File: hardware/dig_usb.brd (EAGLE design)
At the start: 146.1 x 102.6 mm, 123 parts, among them IC201 ATMEGA32A-AU, IC202 DS1337S, IC203 MAX487CSA, IC204 74HC166D, IC205 74HC595D, IC301 LTV-356T, IC302 LTV-356T, IC303 LTV-356T, IC304 LTV-356T, IC305 LTV-356T, IC306 LTV-356T, IC307 LTV-356T, IC308 LTV-356T, K401 S202S02, K402 S202S02, K403 S202S02, K404 S202S02, K405 S202S02, K406 S202S02, K407 S202S02, K408 S202S02, Q201 32,768kHz, T301 BCR191, T302 BCR191, T303 BCR191, T304 BCR191, T305 BCR191, T306 BCR191, T307 BCR191, T308 BCR191, X101 RIA-73-02, X201 ISP, X202 RIA-73-02, X301 RIA-73-02, X302 RIA-73-02, X303 RIA-73-02, X304 RIA-73-02, X305 RIA-73-02, X401 RIA-73-02, X402 RIA-73-02, X403 RIA-73-02, X404 RIA-73-02, X405 RIA-73-02

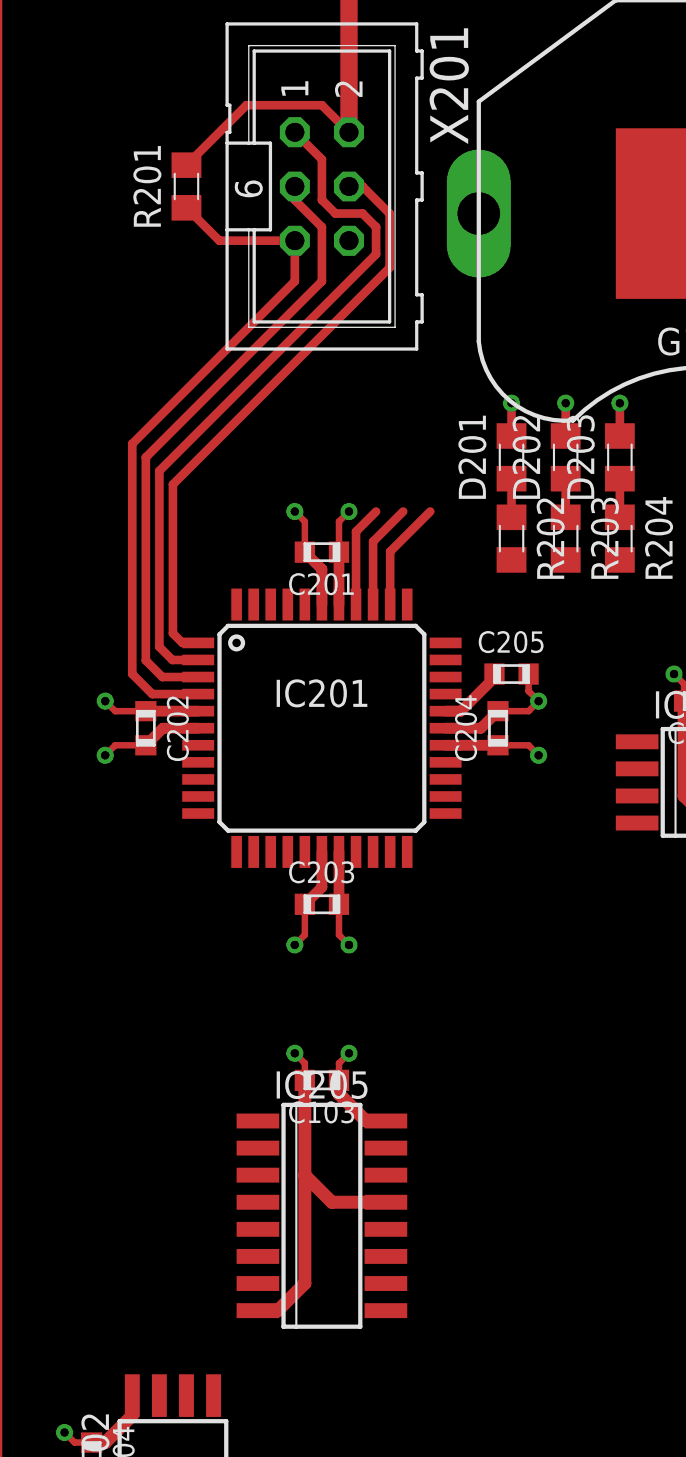
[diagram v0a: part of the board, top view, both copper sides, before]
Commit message: dig_usb auf AT90USB1287 umgestellt
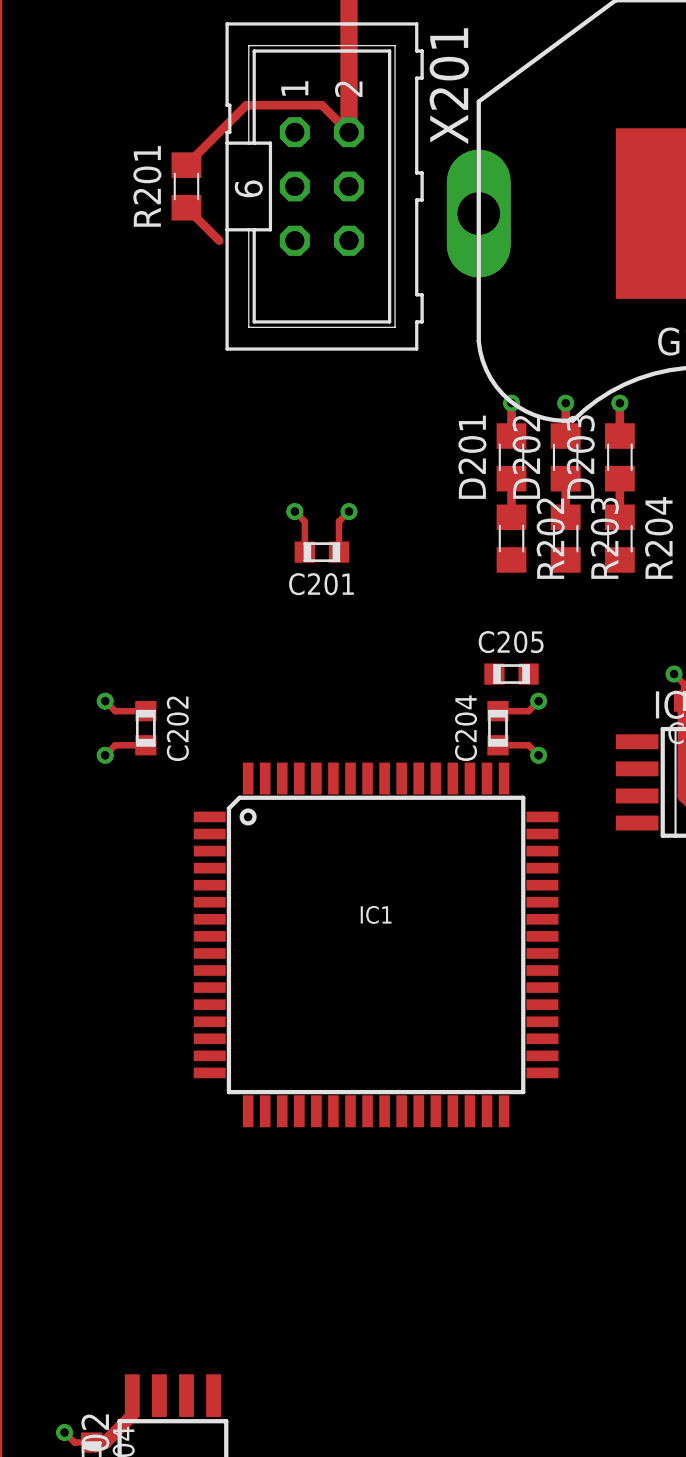
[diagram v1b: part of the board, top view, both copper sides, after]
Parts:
- removed C103, C203: 100nF, passiv:CHIP_0603
- removed IC201: ATMEGA32A-AU, ic-mcu:QFP44_08
- removed IC205: 74HC595D, ic-logik:SOP16_127
- added IC1: AT90USB1287-AU, ic-mcu:QFP64_08
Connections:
- removed net DO: IC201.44, IC205.14
- removed net N$25: C205.1, IC201.29
- removed net N$42: IC201.4, R201.1, X201.RESET
- removed net N$61: IC201.30, R205.1, R206.1
- removed net N$8: IC201.35, R204.2
- removed net N$90: IC201.37, R202.2
- removed net N$92: IC201.36, R203.2
- new net !RESET: IC1.20, R201.1, X201.RESET
- new net LED1: IC1.15, R202.2
- new net LED2: IC1.16, R203.2
- new net LED3: IC1.17, R204.2
- new net N$12: C205.1, IC1.62
- new net OUT0: IC1.51
- new net OUT1: IC1.50
- new net OUT2: IC1.49
- new net OUT3: IC1.48
- new net OUT4: IC1.47
- new net OUT5: IC1.46
- new net OUT6: IC1.45
- new net OUT7: IC1.44
- new net TEMP: IC1.54, R205.1, R206.1
- new net UGND: IC1.6
- new net UVCC: IC1.3
- new net VBUS: IC1.8
- net !R: now also IC1.33; no longer IC201.40, IC205.10
- net +5V: now also IC1.21, IC1.52, IC1.64; no longer C103.1, C203.1, IC201.17, IC201.27, IC201.38, IC201.5, IC205.16
- net ALARM1: now also IC1.18; no longer IC201.11
- net ALARM2: now also IC1.19; no longer IC201.12
- net BAT: now also IC1.55; no longer IC201.31
- net C1: now also IC1.31; no longer IC201.41, IC205.11
- net C2: now also IC1.32; no longer IC201.42, IC205.12
- net DI: now also IC1.34; no longer IC201.43
- net GND: now also IC1.22, IC1.53, IC1.63; no longer C103.2, C203.2, IC201.18, IC201.28, IC201.39, IC201.6, IC205.13, IC205.8
- net IN0: now also IC1.35; no longer IC201.19
- net IN1: now also IC1.36; no longer IC201.20
- net IN2: now also IC1.37; no longer IC201.21
- net IN3: now also IC1.38; no longer IC201.22
- net IN4: now also IC1.39; no longer IC201.23
- net IN5: now also IC1.40; no longer IC201.24
- net IN6: now also IC1.41; no longer IC201.25
- net IN7: now also IC1.42; no longer IC201.26
- net MISO: now also IC1.13; no longer IC201.2
- net MOSI: now also IC1.12; no longer IC201.1
- net RE: now also IC1.30; no longer IC201.14
- net RXD: now also IC1.27; no longer IC201.9
- net SCK: now also IC1.11; no longer IC201.3
- net SCL: now also IC1.25; no longer IC201.15
- net SDA: now also IC1.26; no longer IC201.16
- net TE: now also IC1.29; no longer IC201.13
- net TXD: now also IC1.28; no longer IC201.10
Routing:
- net MISO: track 32.7 -> 0.00 mm
- net N$42: track 32.7 -> 0.00 mm
- net GND: track 93.6 -> 61.2 mm, vias 13 -> 11
- net SCK: track 28.9 -> 0.00 mm
- net MOSI: track 27.7 -> 0.00 mm
- net +5V: track 376.0 -> 359.0 mm, vias 7 -> 5
- net N$8: track 5.14 -> 0.00 mm
- net N$92: track 4.94 -> 0.00 mm
- net N$90: track 4.75 -> 0.00 mm
- net N$25: track 3.11 -> 0.00 mm
- net !RESET: track 0.00 -> 2.18 mm

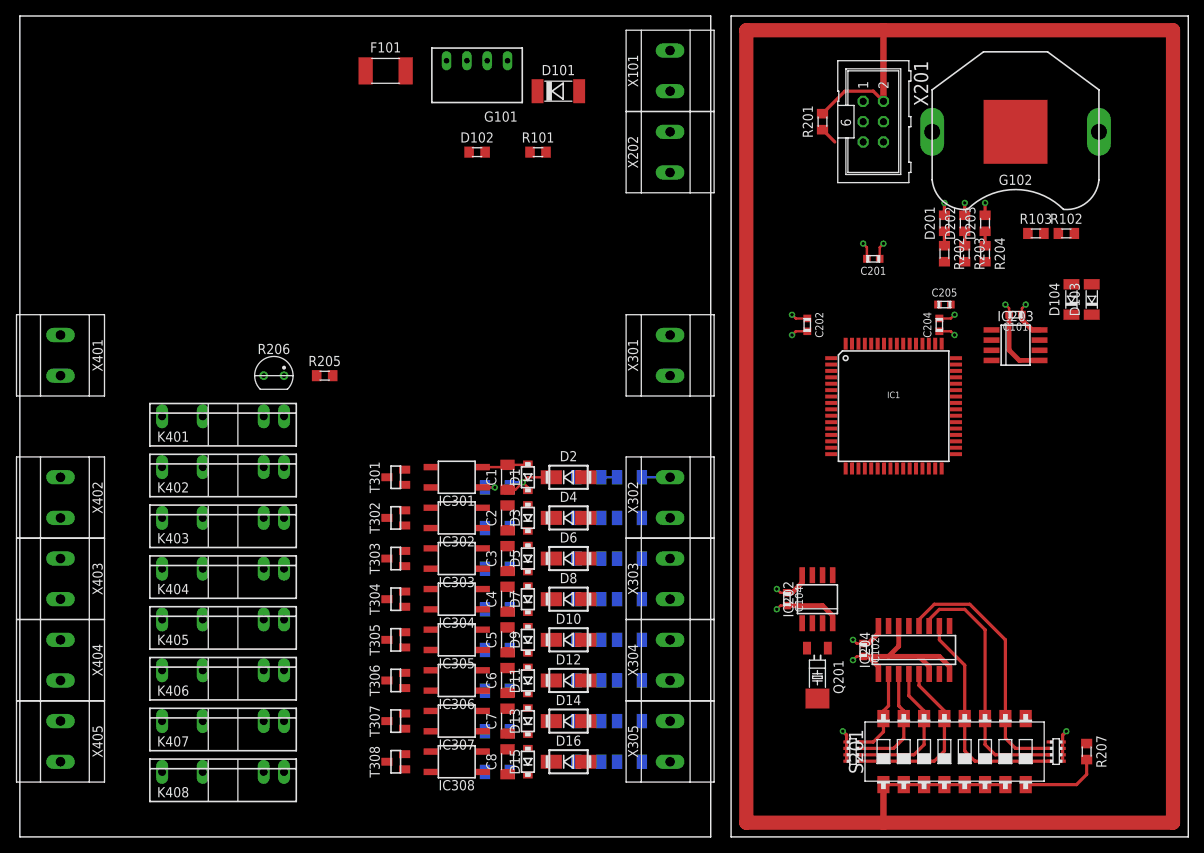
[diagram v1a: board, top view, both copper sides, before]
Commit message: IO Bereich der unteren Platine geroutet
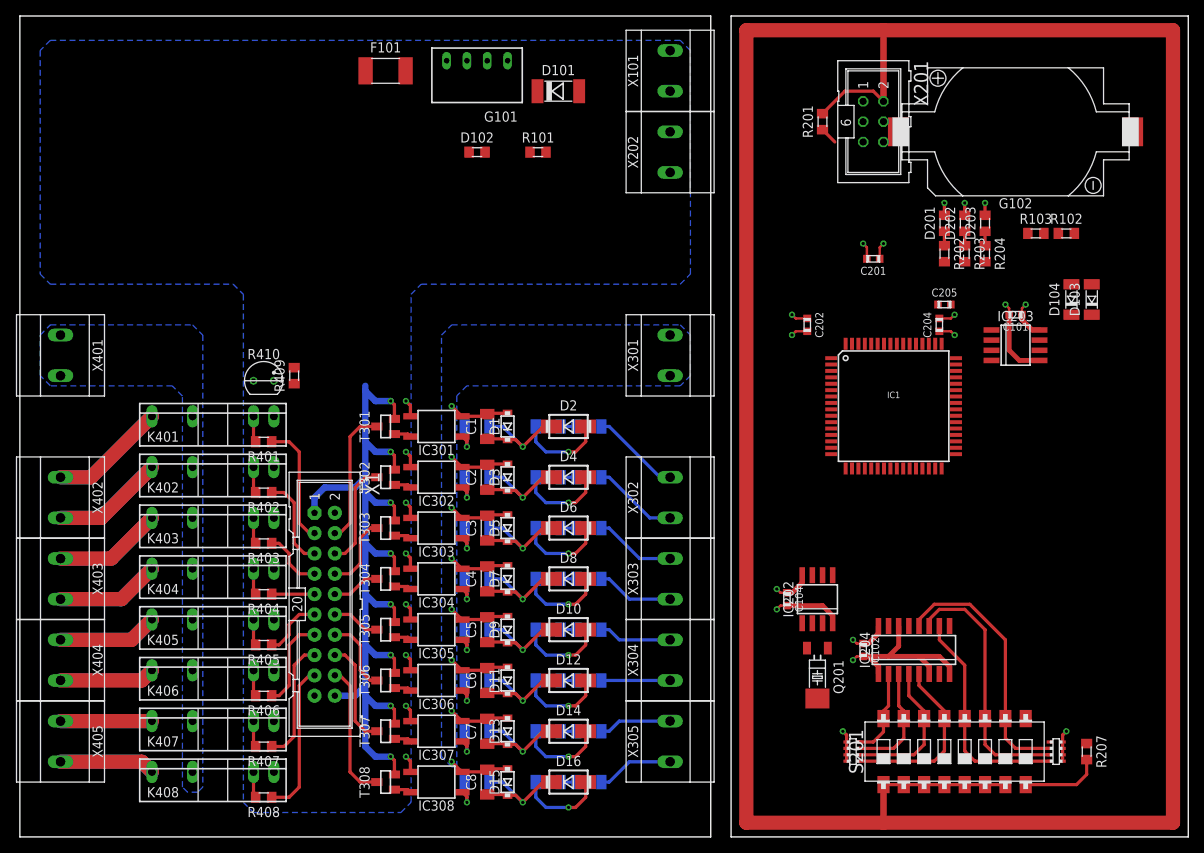
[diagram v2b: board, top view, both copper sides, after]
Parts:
- removed R205: 3,3kΩ, passiv:CHIP_0805
- removed R206: KTY81-210, sensor:TO92
- added R401, R402, R403, R404, R405, R406, R407, R408: (no value), passiv:CHIP_0805
- added R409: 3,3kΩ, passiv:CHIP_0805
- added R410: KTY81-210, sensor:TO92
- added X1: (no value), anschluss:WS20V
- G102: value KZH20P -> KZH20SMD-2; device batterie:KZH20P -> batterie:KHZ20SMD-2
- moved R1 8.13 mm to (66.0, 50.8)
- moved R2 8.13 mm to (71.1, 50.8)
- moved R3 8.03 mm to (57.1, 50.8)
- moved R4 7.18 mm to (66.0, 44.5)
- moved R5 7.18 mm to (71.1, 44.5)
- moved R6 6.84 mm to (57.1, 44.5)
- moved C1 6.84 mm to (58.4, 50.8)
- moved D1 6.84 mm to (61.0, 50.8)
- moved IC301 6.84 mm to (52.1, 50.8)
- moved T301 6.48 mm to (45.7, 50.8)
- moved R7 6.35 mm to (66.0, 38.1)
- moved R8 6.35 mm to (71.1, 38.1)
- moved D2 6.35 mm to (68.6, 50.8)
- moved C2 5.68 mm to (58.4, 44.5)
- moved D3 5.68 mm to (61.0, 44.5)
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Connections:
- new net N$100: T307.3, X1.16
- new net N$101: T308.3, X1.18
- new net N$16: K402.3, R402.2
- new net N$25: K403.3, R403.2
- new net N$37: K404.3, R404.2
- new net N$42: K405.3, R405.2
- new net N$50: K406.3, R406.2
- new net N$61: K407.3, R407.2
- new net N$66: K408.3, R408.2
- new net N$67: R401.1, X1.3
- new net N$79: R402.1, X1.5
- new net N$8: K401.3, R401.2
- new net N$87: R403.1, X1.7
- new net N$88: R404.1, X1.9
- new net N$90: R405.1, X1.11
- new net N$91: R406.1, X1.13
- new net N$92: R407.1, X1.15
- new net N$93: R408.1, X1.17
- new net N$94: T301.3, X1.4
- new net N$95: T302.3, X1.6
- new net N$96: T303.3, X1.8
- new net N$97: T304.3, X1.10
- new net N$98: T305.3, X1.12
- new net N$99: T306.3, X1.14
- net +5V: now also R409.2, X1.1, X1.20; no longer R205.2
- net GND: now also G102.-, R410.2, X1.19, X1.2; no longer G102.N, R206.2
- net IN0: no longer T301.3
- net IN1: no longer T302.3
- net IN2: no longer T303.3
- net IN3: no longer T304.3
- net IN4: no longer T305.3
- net IN5: no longer T306.3
- net IN6: no longer T307.3
- net IN7: no longer T308.3
- net N$21: now also G102.+; no longer G102.P1, G102.P2
- net TEMP: now also R409.1, R410.1; no longer R205.1, R206.1
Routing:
- net +5V: track 359.0 -> 466.6 mm, vias 5 -> 13
- net GNDIO: track 5.80 -> 61.3 mm, vias 0 -> 8
- net N$68: track 0.00 -> 29.2 mm
- net N$72: track 0.00 -> 28.1 mm
- net N$74: track 0.00 -> 27.1 mm
- net N$76: track 0.00 -> 26.0 mm
- net N$78: track 0.00 -> 25.0 mm
- net N$89: track 0.00 -> 23.9 mm
- net N$82: track 0.00 -> 23.9 mm
- net N$84: track 0.00 -> 22.9 mm
- net N$93: track 0.00 -> 19.1 mm
- net N$101: track 0.00 -> 17.1 mm
- net N$94: track 0.00 -> 17.1 mm
- net GND: track 61.2 -> 78.2 mm, vias 11 -> 19
- net N$92: track 0.00 -> 15.3 mm
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- added copper zone on layer 16, net GNDIO
- added copper zone on layer 16, net L

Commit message: Einiges auf dig_usb controllerboard gerouted
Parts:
- removed R101, R202, R203, R204: 390Ω, passiv:CHIP_0805
- added D17, D18, D19, D20, D21, D22, D23, D24, D25, D26, D27, D28, D29, D30, D31, D32: GN, led:CHIP_0805
- added R25, R26, R27, R28, R29: 1,5kΩ, widerstandsnetzwerk:1206
- added X2: (no value), anschluss:WS20V
- R401, R402, R403, R404, R405, R406, R407, R408: value (none) -> 470Ω
- moved Q201 94.1 mm to (22.2, 74.9), turned to 90 degrees
- moved IC202 83.5 mm to (29.8, 74.9), turned to 270 degrees
- moved C104 82.6 mm to (29.8, 78.7), turned to 180 degrees
- moved C101 43.8 mm to (123.2, 21.0), turned to 270 degrees
- moved D102 43.5 mm to (99.7, 76.2), turned to 90 degrees
- moved IC203 40.1 mm to (127.0, 21.0), turned to 0 degrees
- moved C202 23.4 mm to (121.3, 58.4), turned to 90 degrees
- moved D203 18.4 mm to (102.2, 76.2)
- moved D202 13.3 mm to (104.8, 76.2)
- moved R103 12.8 mm to (132.7, 63.5), turned to 90 degrees
- moved R102 12.3 mm to (135.3, 63.5), turned to 90 degrees
- moved C201 9.92 mm to (100.3, 64.1), turned to 270 degrees
- moved IC1 8.35 mm to (110.5, 61.6), turned to 270 degrees
- moved D201 8.25 mm to (107.3, 76.2)
- moved C204 6.87 mm to (120.7, 67.3), turned to 270 degrees
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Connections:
- new net N$102: D17.1, R25.1B
- new net N$103: D18.1, R25.2B
- new net N$104: D19.1, R25.3B
- new net N$105: D20.1, R25.4B
- new net N$106: D21.1, R26.1B
- new net N$107: D22.1, R26.2B
- new net N$108: D23.1, R26.3B
- new net N$109: D24.1, R26.4B
- new net N$110: D25.1, R27.1A
- new net N$111: D26.1, R27.2A
- new net N$112: D27.1, R27.3A
- new net N$113: D28.1, R27.4A
- new net N$114: D29.1, R28.1A
- new net N$115: D30.1, R28.2A
- new net N$116: D31.1, R28.3A
- new net N$117: D32.1, R28.4A
- net +5V: now also R29.4B, X2.1, X2.20; no longer R101.2
- net GND: now also D17.2, D18.2, D19.2, D20.2, D21.2, D22.2, D23.2, D24.2, D25.2, D26.2, D27.2, D28.2, D29.2, D30.2, D31.2, D32.2, X2.19, X2.2
- net IN0: now also R25.1A, X2.4
- net IN1: now also R25.2A, X2.6
- net IN2: now also R25.3A, X2.8
- net IN3: now also R25.4A, X2.10
- net IN4: now also R26.1A, X2.12
- net IN5: now also R26.2A, X2.14
- net IN6: now also R26.3A, X2.16
- net IN7: now also R26.4A, X2.18
- net LED1: now also R29.1B; no longer R202.2
- net LED2: now also R29.2B; no longer R203.2
- net LED3: now also R29.3B; no longer R204.2
- net N$4: now also R29.3A; no longer R204.1
- net N$44: now also R29.4A; no longer R101.1
- net N$62: now also R29.1A; no longer R202.1
- net N$63: now also R29.2A; no longer R203.1
- net OUT0: now also R27.1B, X2.3
- net OUT1: now also R27.2B, X2.5
- net OUT2: now also R27.3B, X2.7
- net OUT3: now also R27.4B, X2.9
- net OUT4: now also R28.1B, X2.11
- net OUT5: now also R28.2B, X2.13
- net OUT6: now also R28.3B, X2.15
- net OUT7: now also R28.4B, X2.17
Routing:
- net +5V: track 466.6 -> 600.6 mm, vias 13 -> 16
- net RXD: track 0.00 -> 83.5 mm, vias 0 -> 2
- net TXD: track 0.00 -> 83.0 mm, vias 0 -> 2
- net TE: track 0.00 -> 78.8 mm, vias 0 -> 2
- net RE: track 0.00 -> 74.7 mm, vias 0 -> 2
- net C1: track 0.00 -> 55.4 mm, vias 0 -> 2
- net GND: track 78.2 -> 130.4 mm
- net OUT7: track 0.00 -> 45.0 mm, vias 0 -> 2
- net IN7: track 0.00 -> 44.1 mm, vias 0 -> 1
- net DI: track 0.00 -> 42.8 mm, vias 0 -> 2
- net OUT6: track 0.00 -> 41.8 mm, vias 0 -> 2
- net !R: track 0.00 -> 40.9 mm, vias 0 -> 2
- net IN6: track 0.00 -> 40.9 mm, vias 0 -> 1
- net C2: track 0.00 -> 39.8 mm, vias 0 -> 2
- net OUT5: track 0.00 -> 39.6 mm, vias 0 -> 2
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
